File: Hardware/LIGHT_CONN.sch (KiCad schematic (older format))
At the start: 46 parts, among them P10 -15V, P11 ~3, P13 ~4, P14 +5V, P18 RX1, P19 3.3V, P20 TX2, P21 1.8V, P22 PSU_CTL, P23 GND, P27 D1, P29 D2, P30 D3, P31 P1, P32 L1.8_1, P33 L3.3_1, P34 P2, P35 L1.8_2, P36 L3.3_2, P37 P3, P38 L1.8_3, P39 L3.3_3, P40 P4, P41 L1.8_4, P42 L3.3_4, P6 CONN_02X14, P7 ~5, P8 +15V, P9 ~6, U22 PCA9685BS

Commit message: Routing split rail DC/DC converter
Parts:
- U22: footprint Housings_DFN_QFN:QFN-28-1EP_6x6mm_Pitch0.65mm -> muse-v2-lib:QFN-28-1EP_6x6mm_Pitch0.65mm_THERMAL
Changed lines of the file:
@@
 F 0 "U22" H 2150 1200 60  0000 C CNN
 F 1 "PCA9685BS" H 2750 -600 60  0000 C CNN
-F 2 "Housings_DFN_QFN:QFN-28-1EP_6x6mm_Pitch0.65mm" H 3000 650 60  0001 C CNN
+F 2 "muse-v2-lib:QFN-28-1EP_6x6mm_Pitch0.65mm_THERMAL" H 3000 650 60  0001 C CNN
 F 3 "" H 3000 650 60  0001 C CNN
 	1    2100 1150

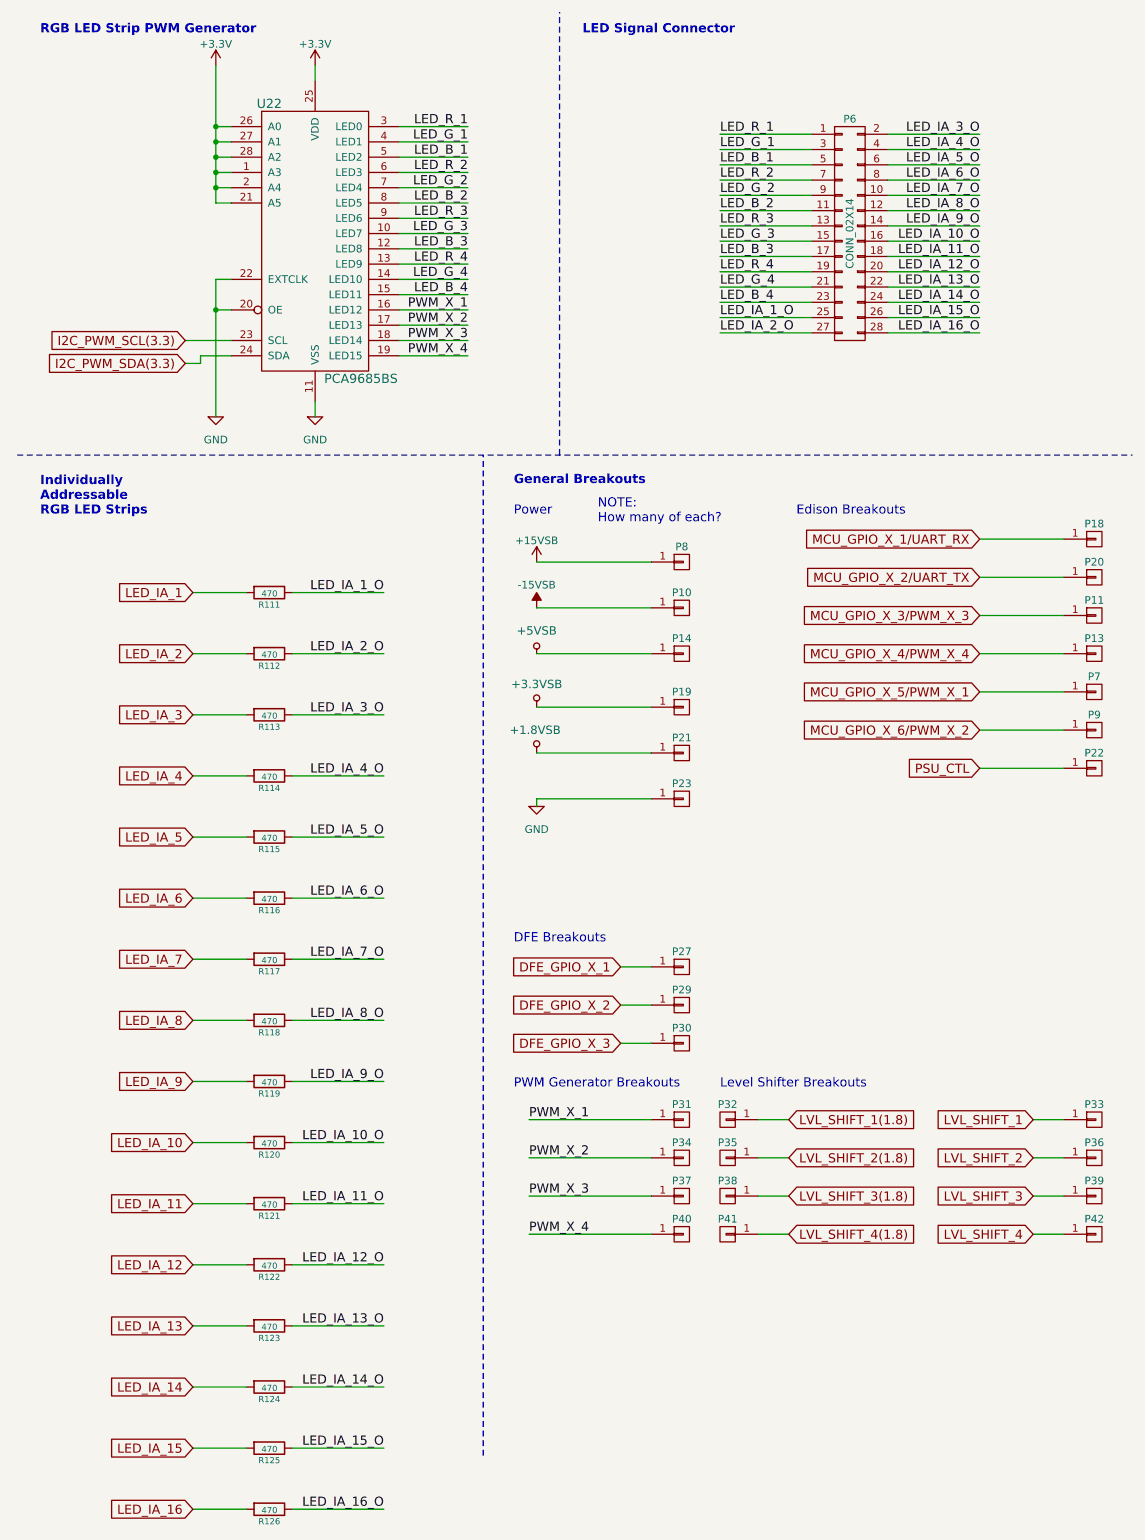
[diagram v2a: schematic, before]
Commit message: Completed placement of level shifters
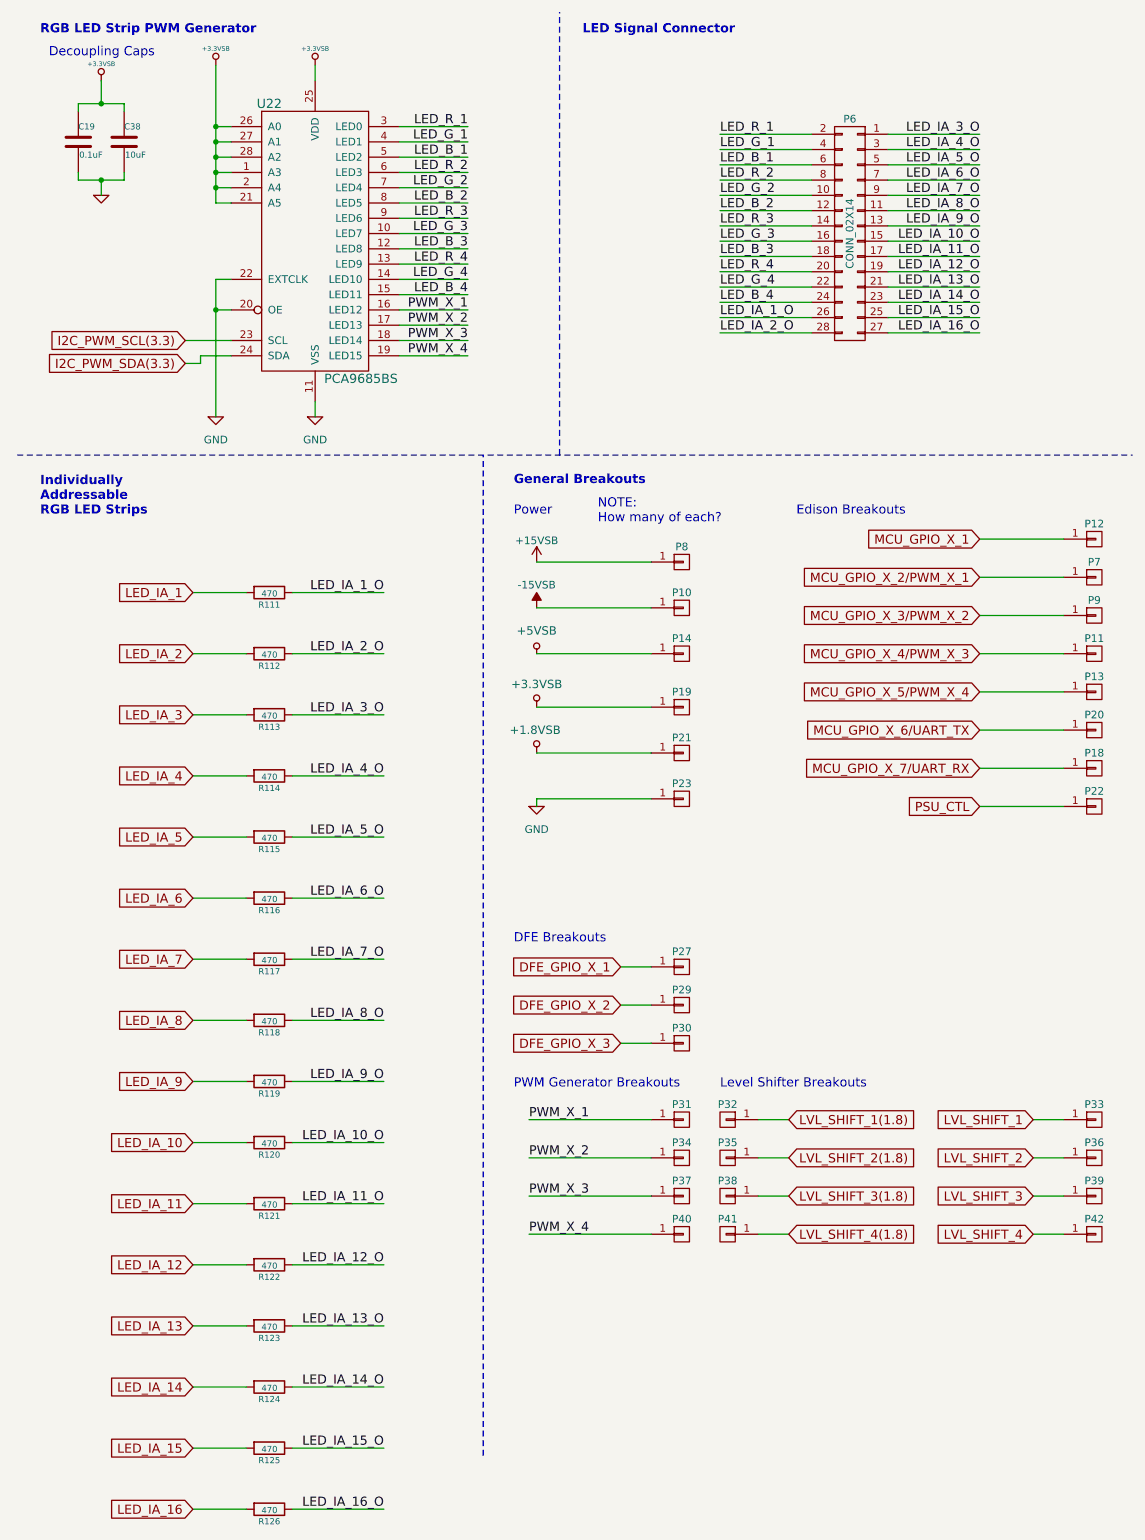
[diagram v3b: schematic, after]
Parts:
- added C19: 0.1uF, Capacitors_SMD:C_0402, symbol C
- added C38: 10uF, Capacitors_SMD:C_1206, symbol C
- added P12: 1, Pin_Headers:Pin_Header_Straight_1x01, symbol CONN_01X01
- P11: value ~3 -> ~4
- P13: value ~4 -> ~5
- P18: value RX1 -> RX7
- P20: value TX2 -> TX6
- P7: value ~5 -> ~2
- P9: value ~6 -> ~3
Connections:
- net +3V3 is gone; now on net +3.3VSB: U22.1 (A3), U22.2 (A4), U22.21 (A5), U22.25 (VDD), U22.26 (A0), U22.27 (A1), U22.28 (A2)
- net +3.3VSB: now also C19.1, C38.1
- net GND: now also C19.2, C38.2
- net LED_B_1: now also P6.6 (P6); no longer P6.5 (P5)
- net LED_B_2: now also P6.12 (P12); no longer P6.11 (P11)
- net LED_B_3: now also P6.18 (P18); no longer P6.17 (P17)
- net LED_B_4: now also P6.24 (P24); no longer P6.23 (P23)
- net LED_G_1: now also P6.4 (P4); no longer P6.3 (P3)
- net LED_G_2: now also P6.10 (P10); no longer P6.9 (P9)
- net LED_G_3: now also P6.16 (P16); no longer P6.15 (P15)
- net LED_G_4: now also P6.22 (P22); no longer P6.21 (P21)
- net LED_IA_10_O: now also P6.15 (P15); no longer P6.16 (P16)
- net LED_IA_11_O: now also P6.17 (P17); no longer P6.18 (P18)
- net LED_IA_12_O: now also P6.19 (P19); no longer P6.20 (P20)
- net LED_IA_13_O: now also P6.21 (P21); no longer P6.22 (P22)
- net LED_IA_14_O: now also P6.23 (P23); no longer P6.24 (P24)
- net LED_IA_15_O: now also P6.25 (P25); no longer P6.26 (P26)
- net LED_IA_16_O: now also P6.27 (P27); no longer P6.28 (P28)
- net LED_IA_1_O: now also P6.26 (P26); no longer P6.25 (P25)
- net LED_IA_2_O: now also P6.28 (P28); no longer P6.27 (P27)
- net LED_IA_3_O: now also P6.1 (P1); no longer P6.2 (P2)
- net LED_IA_4_O: now also P6.3 (P3); no longer P6.4 (P4)
- net LED_IA_5_O: now also P6.5 (P5); no longer P6.6 (P6)
- net LED_IA_6_O: now also P6.7 (P7); no longer P6.8 (P8)
- net LED_IA_7_O: now also P6.9 (P9); no longer P6.10 (P10)
- net LED_IA_8_O: now also P6.11 (P11); no longer P6.12 (P12)
- net LED_IA_9_O: now also P6.13 (P13); no longer P6.14 (P14)
- net LED_R_1: now also P6.2 (P2); no longer P6.1 (P1)
- net LED_R_2: now also P6.8 (P8); no longer P6.7 (P7)
- net LED_R_3: now also P6.14 (P14); no longer P6.13 (P13)
- net LED_R_4: now also P6.20 (P20); no longer P6.19 (P19)
- net MCU_GPIO_X_1/UART_RX renamed MCU_GPIO_X_7/UART_RX
- net MCU_GPIO_X_2/UART_TX renamed MCU_GPIO_X_6/UART_TX
- net MCU_GPIO_X_3/PWM_X_3 renamed MCU_GPIO_X_4/PWM_X_3
- net MCU_GPIO_X_4/PWM_X_4 renamed MCU_GPIO_X_5/PWM_X_4
- net MCU_GPIO_X_5/PWM_X_1 renamed MCU_GPIO_X_2/PWM_X_1
- net MCU_GPIO_X_6/PWM_X_2 renamed MCU_GPIO_X_3/PWM_X_2
- new net MCU_GPIO_X_1: P12.1 (P1)
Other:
- note added: "Decoupling Caps"
- moved on the sheet: P11, P13, P18, P20, P22, P7, P9
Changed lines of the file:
@@
-	1    0    0    -1
-$EndComp
-$Comp
-L +3.3V-RESCUE-museV2 #PWR0119
-U 1 1 57E6273F
-P 2450 850
-F 0 "#PWR0119" H 2450 700 50  0001 C CNN
-F 1 "+3.3V" H 2450 990 50  0000 C CNN
-F 2 "" H 2450 850 50  0000 C CNN
-F 3 "" H 2450 850 50  0000 C CNN
-	1    2450 850
 	1    0    0    -1
 $EndComp
@@
 Text Notes 650  650  0    60   ~ 12
 RGB LED Strip PWM Generator
-$Comp
-L +3.3V-RESCUE-museV2 #PWR0120
-U 1 1 57EA76FD
-P 1800 850
-F 0 "#PWR0120" H 1800 700 50  0001 C CNN
-F 1 "+3.3V" H 1800 990 50  0000 C CNN
-F 2 "" H 1800 850 50  0000 C CNN
-F 3 "" H 1800 850 50  0000 C CNN
-	1    1800 850
-	1    0    0    -1
-$EndComp
 Wire Wire Line
 	1800 850  1800 1750
@@
 Connection ~ 1800 1250
 $Comp
-L GND-RESCUE-museV2-RESCUE-museV2 #PWR0121
+L GND-RESCUE-museV2-RESCUE-museV2 #PWR0119
 U 1 1 57EF1660
 P 1800 3150
-F 0 "#PWR0121" H 1800 2900 50  0001 C CNN
+F 0 "#PWR0119" H 1800 2900 50  0001 C CNN
 F 1 "GND" H 1800 3000 50  0000 C CNN
 F 2 "" H 1800 3150 50  0000 C CNN
@@
 F 3 "" H 5950 800 50  0000 C CNN
 	1    5950 1950
-	1    0    0    -1
+	-1   0    0    -1
 $EndComp
 Text Label 5100 1500 0    60   ~ 0
@@
 $EndComp
 $Comp
-L +15VSB #PWR0122
+L +15VSB #PWR0120
 U 1 1 57FFBADE
 P 3900 4100
-F 0 "#PWR0122" H 3900 3950 50  0001 C CNN
+F 0 "#PWR0120" H 3900 3950 50  0001 C CNN
 F 1 "+15VSB" H 3900 4240 50  0000 C CNN
 F 2 "" H 3900 4100 50  0000 C CNN
@@
 	4650 4400 3900 4400
 $Comp
-L -15VSB #PWR132
+L -15VSB #PWR134
 U 1 1 57FFBC18
 P 3900 4400
-F 0 "#PWR132" H 3900 4500 50  0001 C CNN
+F 0 "#PWR134" H 3900 4500 50  0001 C CNN
 F 1 "-15VSB" H 3900 4550 50  0000 C CNN
 F 2 "" H 3900 4400 50  0000 C CNN
@@
 	4650 4700 3900 4700
 $Comp
-L +5VSB #PWR0123
+L +5VSB #PWR0121
 U 1 1 57FFD044
 P 3900 4700
-F 0 "#PWR0123" H 3900 4790 20  0001 C CNN
+F 0 "#PWR0121" H 3900 4790 20  0001 C CNN
 F 1 "+5VSB" H 3900 4850 55  0000 C CNN
 F 2 "" H 3900 4700 60  0000 C CNN
@@
 	4650 5050 3900 5050
 $Comp
-L +3.3VSB #PWR0124
+L +3.3VSB #PWR0122
 U 1 1 57FFEA10
 P 3900 5050
-F 0 "#PWR0124" H 3900 5010 30  0001 C CNN
+F 0 "#PWR0122" H 3900 5010 30  0001 C CNN
 F 1 "+3.3VSB" H 3900 5200 55  0000 C CNN
 F 2 "" H 3900 5050 60  0000 C CNN
@@
 	4650 5350 3900 5350
 $Comp
-L +1.8VSB #PWR0125
+L +1.8VSB #PWR0123
 U 1 1 57FFEE42
 P 3900 5350
-F 0 "#PWR0125" H 3900 5490 20  0001 C CNN
+F 0 "#PWR0123" H 3900 5490 20  0001 C CNN
 F 1 "+1.8VSB" H 3890 5500 55  0000 C CNN
 F 2 "" H 3900 5350 60  0000 C CNN
@@
 	4650 5650 3900 5650
 $Comp
-L GND-RESCUE-museV2-RESCUE-museV2 #PWR0126
+L GND-RESCUE-museV2-RESCUE-museV2 #PWR0124
 U 1 1 57FFF105
 P 3900 5700
-F 0 "#PWR0126" H 3900 5450 50  0001 C CNN
+F 0 "#PWR0124" H 3900 5450 50  0001 C CNN
 F 1 "GND" H 3900 5550 50  0000 C CNN
 F 2 "" H 3900 5700 50  0000 C CNN
@@
 L CONN_01X01 P11
 U 1 1 58006FC1
+P 7550 4700
+F 0 "P11" H 7550 4800 50  0000 C CNN
+F 1 "~4" V 7650 4700 50  0001 C CNN
+F 2 "Pin_Headers:Pin_Header_Straight_1x01" H 7550 4700 50  0001 C CNN
+F 3 "" H 7550 4700 50  0000 C CNN
+	1    7550 4700
+	1    0    0    -1
+$EndComp
+$Comp
+L CONN_01X01 P9
+U 1 1 58006FC7
 P 7550 4450
-F 0 "P11" H 7550 4550 50  0000 C CNN
+F 0 "P9" H 7550 4550 50  0000 C CNN
 F 1 "~3" V 7650 4450 50  0001 C CNN
 F 2 "Pin_Headers:Pin_Header_Straight_1x01" H 7550 4450 50  0001 C CNN
@@
 $EndComp
 $Comp
-L CONN_01X01 P9
-U 1 1 58006FC7
-P 7550 5200
-F 0 "P9" H 7550 5300 50  0000 C CNN
-F 1 "~6" V 7650 5200 50  0001 C CNN
-F 2 "Pin_Headers:Pin_Header_Straight_1x01" H 7550 5200 50  0001 C CNN
-F 3 "" H 7550 5200 50  0000 C CNN
-	1    7550 5200
-	1    0    0    -1
-$EndComp
-$Comp
 L CONN_01X01 P7
 U 1 1 58006FCD
+P 7550 4200
+F 0 "P7" H 7550 4300 50  0000 C CNN
+F 1 "~2" V 7650 4200 50  0001 C CNN
+F 2 "Pin_Headers:Pin_Header_Straight_1x01" H 7550 4200 50  0001 C CNN
+F 3 "" H 7550 4200 50  0000 C CNN
+	1    7550 4200
+	1    0    0    -1
+$EndComp
+Wire Wire Line
+	6800 4200 7350 4200
+Wire Wire Line
+	7350 4450 6800 4450
+Wire Wire Line
+	6800 4700 7350 4700
+$Comp
+L CONN_01X01 P13
+U 1 1 58007233
 P 7550 4950
-F 0 "P7" H 7550 5050 50  0000 C CNN
+F 0 "P13" H 7550 5050 50  0000 C CNN
 F 1 "~5" V 7650 4950 50  0001 C CNN
 F 2 "Pin_Headers:Pin_Header_Straight_1x01" H 7550 4950 50  0001 C CNN
@@
 Wire Wire Line
 	6800 4950 7350 4950
-Wire Wire Line
-	7350 5200 6800 5200
-Wire Wire Line
-	6800 4450 7350 4450
-$Comp
-L CONN_01X01 P13
-U 1 1 58007233
-P 7550 4700
-F 0 "P13" H 7550 4800 50  0000 C CNN
-F 1 "~4" V 7650 4700 50  0001 C CNN
-F 2 "Pin_Headers:Pin_Header_Straight_1x01" H 7550 4700 50  0001 C CNN
-F 3 "" H 7550 4700 50  0000 C CNN
-	1    7550 4700
-	1    0    0    -1
-$EndComp
-Wire Wire Line
-	6800 4700 7350 4700
-Text GLabel 6800 4700 0    60   Input ~ 0
-MCU_GPIO_X_4/PWM_X_4
-Text GLabel 6800 3950 0    60   Input ~ 0
-MCU_GPIO_X_1/UART_RX
+Text GLabel 6800 4950 0    60   Input ~ 0
+MCU_GPIO_X_5/PWM_X_4
+Text GLabel 6800 5450 0    60   Input ~ 0
+MCU_GPIO_X_7/UART_RX
 $Comp
 L CONN_01X01 P20
 U 1 1 58007A71
-P 7550 4200
-F 0 "P20" H 7550 4300 50  0000 C CNN
-F 1 "TX2" V 7650 4200 50  0001 C CNN
-F 2 "Pin_Headers:Pin_Header_Straight_1x01" H 7550 4200 50  0001 C CNN
-F 3 "" H 7550 4200 50  0000 C CNN
-	1    7550 4200
+P 7550 5200
+F 0 "P20" H 7550 5300 50  0000 C CNN
+F 1 "TX6" V 7650 5200 50  0001 C CNN
+F 2 "Pin_Headers:Pin_Header_Straight_1x01" H 7550 5200 50  0001 C CNN
+F 3 "" H 7550 5200 50  0000 C CNN
+	1    7550 5200
 	1    0    0    -1
 $EndComp
@@
 L CONN_01X01 P18
 U 1 1 58007A77
-P 7550 3950
-F 0 "P18" H 7550 4050 50  0000 C CNN
-F 1 "RX1" V 7650 3950 50  0001 C CNN
-F 2 "Pin_Headers:Pin_Header_Straight_1x01" H 7550 3950 50  0001 C CNN
-F 3 "" H 7550 3950 50  0000 C CNN
-	1    7550 3950
-	1    0    0    -1
-$EndComp
-Wire Wire Line
-	6800 3950 7350 3950
-Wire Wire Line
-	7350 4200 6800 4200
-Text GLabel 6800 4200 0    60   Input ~ 0
-MCU_GPIO_X_2/UART_TX
+P 7550 5450
+F 0 "P18" H 7550 5550 50  0000 C CNN
+F 1 "RX7" V 7650 5450 50  0001 C CNN
+F 2 "Pin_Headers:Pin_Header_Straight_1x01" H 7550 5450 50  0001 C CNN
+F 3 "" H 7550 5450 50  0000 C CNN
+	1    7550 5450
+	1    0    0    -1
+$EndComp
+Wire Wire Line
+	6800 5450 7350 5450
+Wire Wire Line
+	7350 5200 6800 5200
+Text GLabel 6800 5200 0    60   Input ~ 0
+MCU_GPIO_X_6/UART_TX
 Wire Wire Line
 	4450 6750 4650 6750
@@
 Text Label 3850 8500 0    60   ~ 0
 PWM_X_4
+Text GLabel 6800 4700 0    60   Input ~ 0
+MCU_GPIO_X_4/PWM_X_3
 Text GLabel 6800 4450 0    60   Input ~ 0
-MCU_GPIO_X_3/PWM_X_3
-Text GLabel 6800 5200 0    60   Input ~ 0
-MCU_GPIO_X_6/PWM_X_2
-Text GLabel 6800 4950 0    60   Input ~ 0
-MCU_GPIO_X_5/PWM_X_1
+MCU_GPIO_X_3/PWM_X_2
+Text GLabel 6800 4200 0    60   Input ~ 0
+MCU_GPIO_X_2/PWM_X_1
 $Comp
 L CONN_01X01 P22
 U 1 1 585A0CF3
-P 7550 5450
-F 0 "P22" H 7550 5550 50  0000 C CNN
-F 1 "PSU_CTL" V 7650 5450 50  0001 C CNN
-F 2 "Pin_Headers:Pin_Header_Straight_1x01" H 7550 5450 50  0001 C CNN
-F 3 "" H 7550 5450 50  0000 C CNN
-	1    7550 5450
-	1    0    0    -1
-$EndComp
-Wire Wire Line
-	7350 5450 6800 5450
-Text GLabel 6800 5450 0    60   Input ~ 0
+P 7550 5700
+F 0 "P22" H 7550 5800 50  0000 C CNN
+F 1 "PSU_CTL" V 7650 5700 50  0001 C CNN
+F 2 "Pin_Headers:Pin_Header_Straight_1x01" H 7550 5700 50  0001 C CNN
+F 3 "" H 7550 5700 50  0000 C CNN
+	1    7550 5700
+	1    0    0    -1
+$EndComp
+Wire Wire Line
+	7350 5700 6800 5700
+Text GLabel 6800 5700 0    60   Input ~ 0
 PSU_CTL
+Text GLabel 6800 3950 0    60   Input ~ 0
+MCU_GPIO_X_1
+$Comp
+L CONN_01X01 P12
+U 1 1 5862A3DE
+P 7550 3950
+F 0 "P12" H 7550 4050 50  0000 C CNN
+F 1 "1" V 7650 3950 50  0001 C CNN
+F 2 "Pin_Headers:Pin_Header_Straight_1x01" H 7550 3950 50  0001 C CNN
+F 3 "" H 7550 3950 50  0000 C CNN
+	1    7550 3950
+	1    0    0    -1
+$EndComp
+Wire Wire Line
+	7350 3950 6800 3950
+$Comp
+L +3.3VSB #PWR0125
+U 1 1 5862B130
+P 1800 850
+F 0 "#PWR0125" H 1800 810 30  0001 C CNN
+F 1 "+3.3VSB" H 1800 960 30  0000 C CNN
+F 2 "" H 1800 850 60  0000 C CNN
+F 3 "" H 1800 850 60  0000 C CNN
+	1    1800 850
+	1    0    0    -1
+$EndComp
+$Comp
+L +3.3VSB #PWR0126
+U 1 1 5862B1CF
+P 2450 850
+F 0 "#PWR0126" H 2450 810 30  0001 C CNN
+F 1 "+3.3VSB" H 2450 960 30  0000 C CNN
+F 2 "" H 2450 850 60  0000 C CNN
+F 3 "" H 2450 850 60  0000 C CNN
+	1    2450 850
+	1    0    0    -1
+$EndComp
+$Comp
+L C C19
+U 1 1 5862D09E
+P 900 1350
+F 0 "C19" H 900 1450 40  0000 L CNN
+F 1 "0.1uF" H 906 1265 40  0000 L CNN
+F 2 "Capacitors_SMD:C_0402" H 938 1200 30  0001 C CNN
+F 3 "" H 900 1350 60  0000 C CNN
+	1    900  1350
+	1    0    0    -1
+$EndComp
+$Comp
+L C C38
+U 1 1 5862D15A
+P 1200 1350
+F 0 "C38" H 1200 1450 40  0000 L CNN
+F 1 "10uF" H 1206 1265 40  0000 L CNN
+F 2 "Capacitors_SMD:C_1206" H 1238 1200 30  0001 C CNN
+F 3 "" H 1200 1350 60  0000 C CNN
+	1    1200 1350
+	1    0    0    -1
+$EndComp
+$Comp
+L +3.3VSB #PWR0127
+U 1 1 5862D3DB
+P 1050 950
+F 0 "#PWR0127" H 1050 910 30  0001 C CNN
+F 1 "+3.3VSB" H 1050 1060 30  0000 C CNN
+F 2 "" H 1050 950 60  0000 C CNN
+F 3 "" H 1050 950 60  0000 C CNN
+	1    1050 950
+	1    0    0    -1
+$EndComp
+Wire Wire Line
+	900  1150 900  1100
+Wire Wire Line
+	900  1100 1200 1100
+Wire Wire Line
+	1200 1100 1200 1150
+Wire Wire Line
+	1050 1100 1050 950
+Connection ~ 1050 1100
+Wire Wire Line
+	900  1550 900  1600
+Wire Wire Line
+	900  1600 1200 1600
+Wire Wire Line
+	1200 1600 1200 1550
+$Comp
+L GND #PWR0128
+U 1 1 5862D6A9
+P 1050 1700
+F 0 "#PWR0128" H 1050 1700 30  0001 C CNN
+F 1 "GND" H 1050 1630 30  0001 C CNN
+F 2 "" H 1050 1700 60  0000 C CNN
+F 3 "" H 1050 1700 60  0000 C CNN
+	1    1050 1700
+	1    0    0    -1
+$EndComp
+Wire Wire Line
+	1050 1700 1050 1600
+Connection ~ 1050 1600
+Text Notes 1400 800  2    60   ~ 0
+Decoupling Caps
 $EndSCHEMATC
